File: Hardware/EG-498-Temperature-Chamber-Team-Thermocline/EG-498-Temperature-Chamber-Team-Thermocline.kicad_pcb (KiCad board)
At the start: 2 copper layers, 32 x 47 mm, 6 parts, among them J1 Disp_Connector, J2 HMI_Daughter_Connector

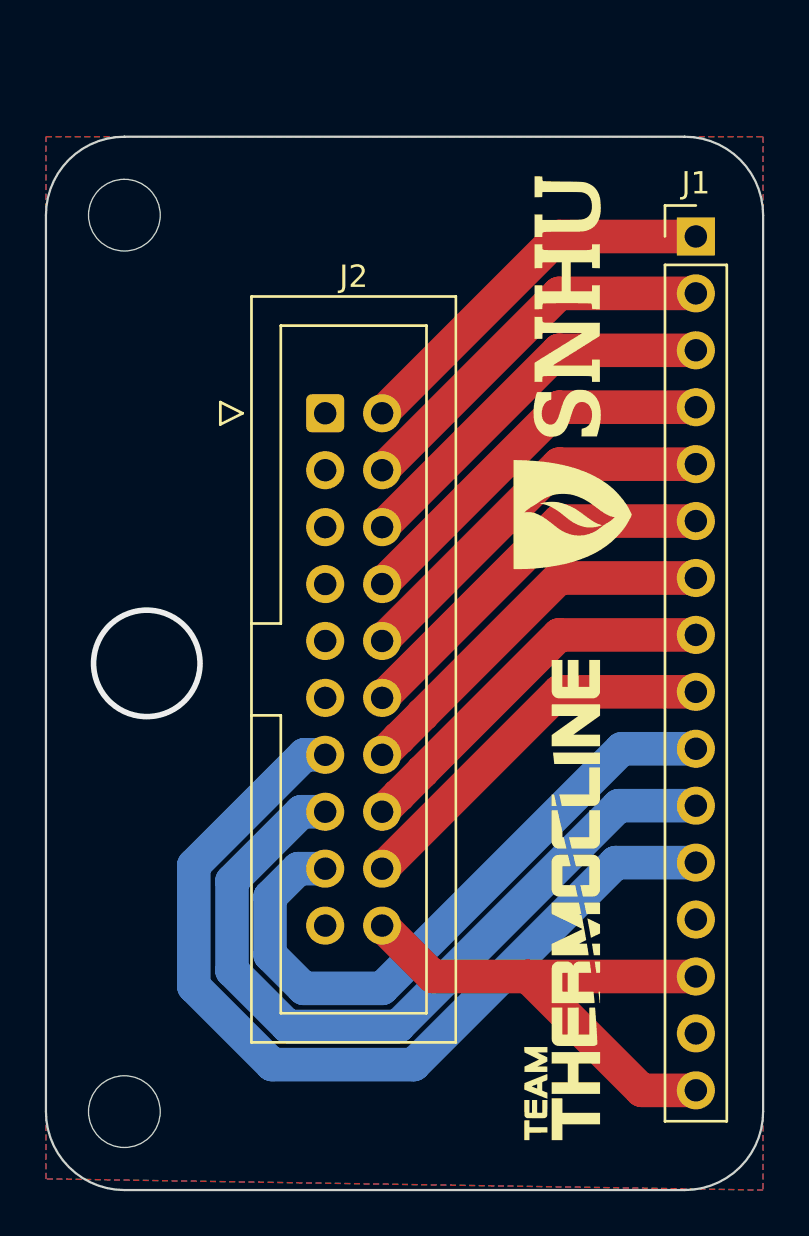
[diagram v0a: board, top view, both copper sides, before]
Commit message: Add knockout
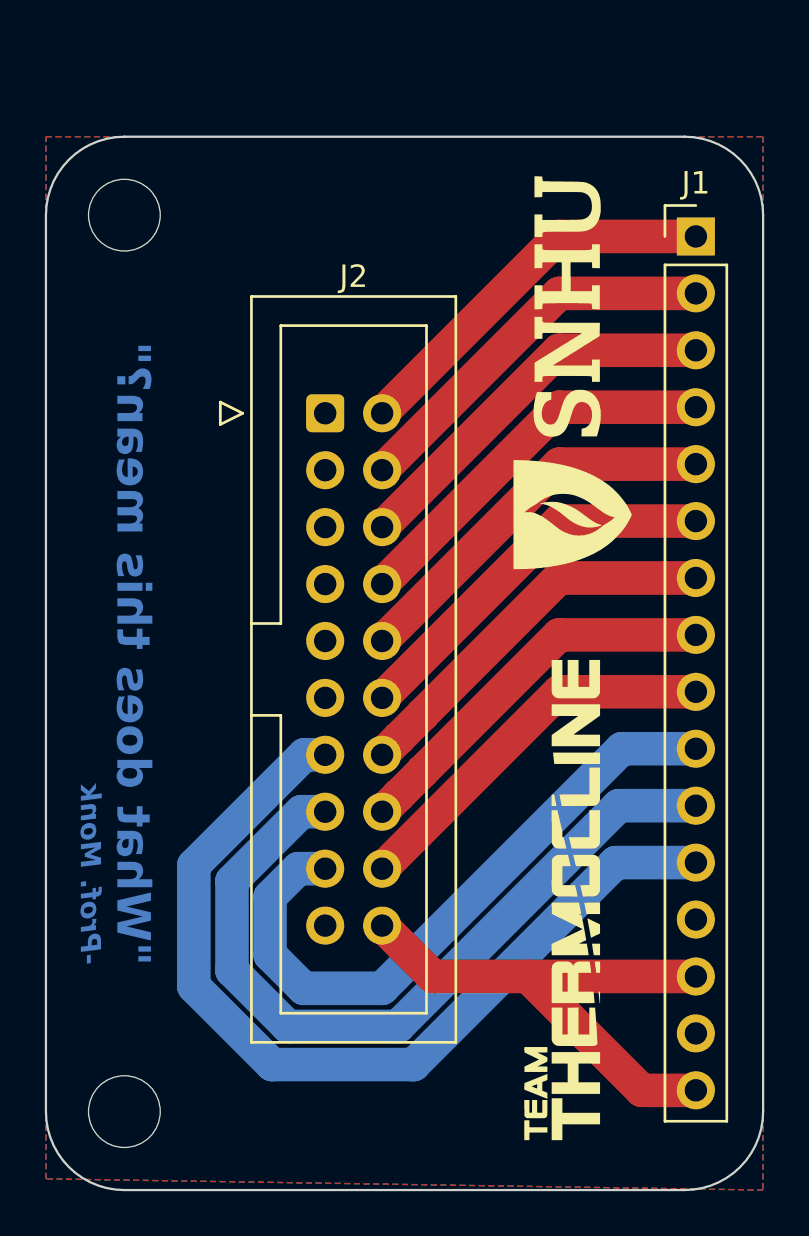
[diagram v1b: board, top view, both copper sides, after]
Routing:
- net (no net): vias 1 -> 0
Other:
- board text added: "-Prof. Monk"
- board text added: "{dblquote}What does this mean?{dblquote}"
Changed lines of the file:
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@@
 		(layer "Edge.Cuts")
 	)
-	(via
-		(at -19 0)
-		(size 5)
-		(drill 4.5)
-		(layers "F.Cu" "B.Cu")
-		(net 0)
+	(gr_text "-Prof. Monk"
+		(at -21 13.5 270)
+		(layer "B.Cu" knockout)
+		(effects
+			(font
+				(size 0.9 0.9)
+				(thickness 0.18)
+				(bold yes)
+				(italic yes)
+			)
+			(justify left top mirror)
+		)
+	)
+	(gr_text "{dblquote}What does this mean?{dblquote}"
+		(at -20.5 13.5 270)
+		(layer "B.Cu" knockout)
+		(effects
+			(font
+				(size 1.5 1.5)
+				(thickness 0.3)
+				(bold yes)
+			)
+			(justify left bottom mirror)
+		)
 	)
 	(segment

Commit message: Add rounded tracks
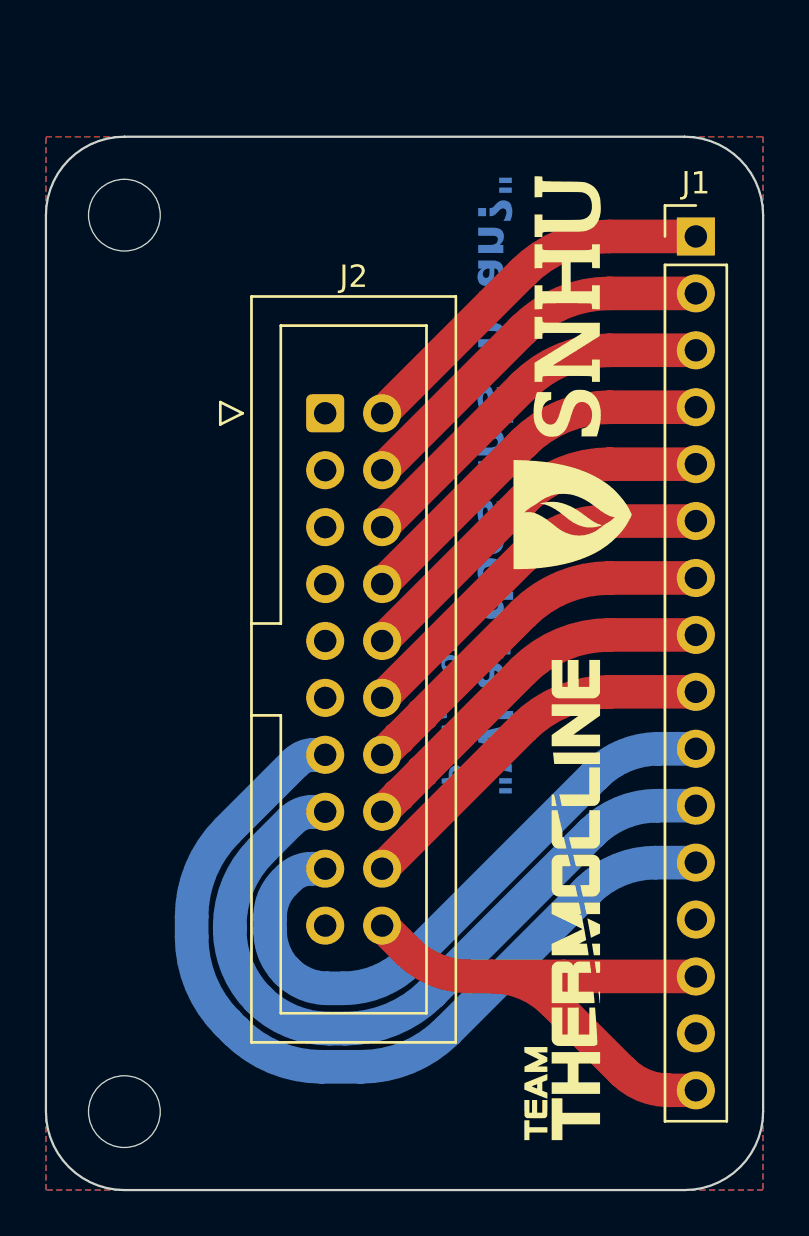
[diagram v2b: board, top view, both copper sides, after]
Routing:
- net +3.3V: track 24.5 -> 27.1 mm
- net /GP28/ADC2: track 40.9 -> 39.9 mm
- net /GP27/ADC1/I2C1_SCL: track 35.2 -> 34.3 mm
- net /GP26/ADC0/I2C1_SDA: track 29.6 -> 28.8 mm
